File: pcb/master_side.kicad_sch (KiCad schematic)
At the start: 109 parts, among them IC1 PCA9956BTWY, J2 4P4C, J4 USB_C_Receptacle_USB2.0_16P, SW1 SW_Push_45deg, SW10 SW_Push_45deg, SW11 SW_Push_45deg, SW12 SW_Push_45deg, SW13 SW_Push_45deg, SW14 SW_Push_45deg, SW15 SW_Push_45deg, SW16 SW_Push_45deg, SW17 SW_Push_45deg, SW18 SW_Push_45deg, SW2 SW_Push_45deg, SW3 SW_Push_45deg, SW4 SW_Push_45deg, SW5 SW_Push_45deg, SW6 SW_Push_45deg, SW7 SW_Push_45deg, SW8 SW_Push_45deg, SW9 SW_Push_45deg, U1 W25Q128JVSIQ, U2 RP2040, U3 NCP1117LPST33T3G, U4 OPT3001DNPR, Y1 ABM8-272-T3

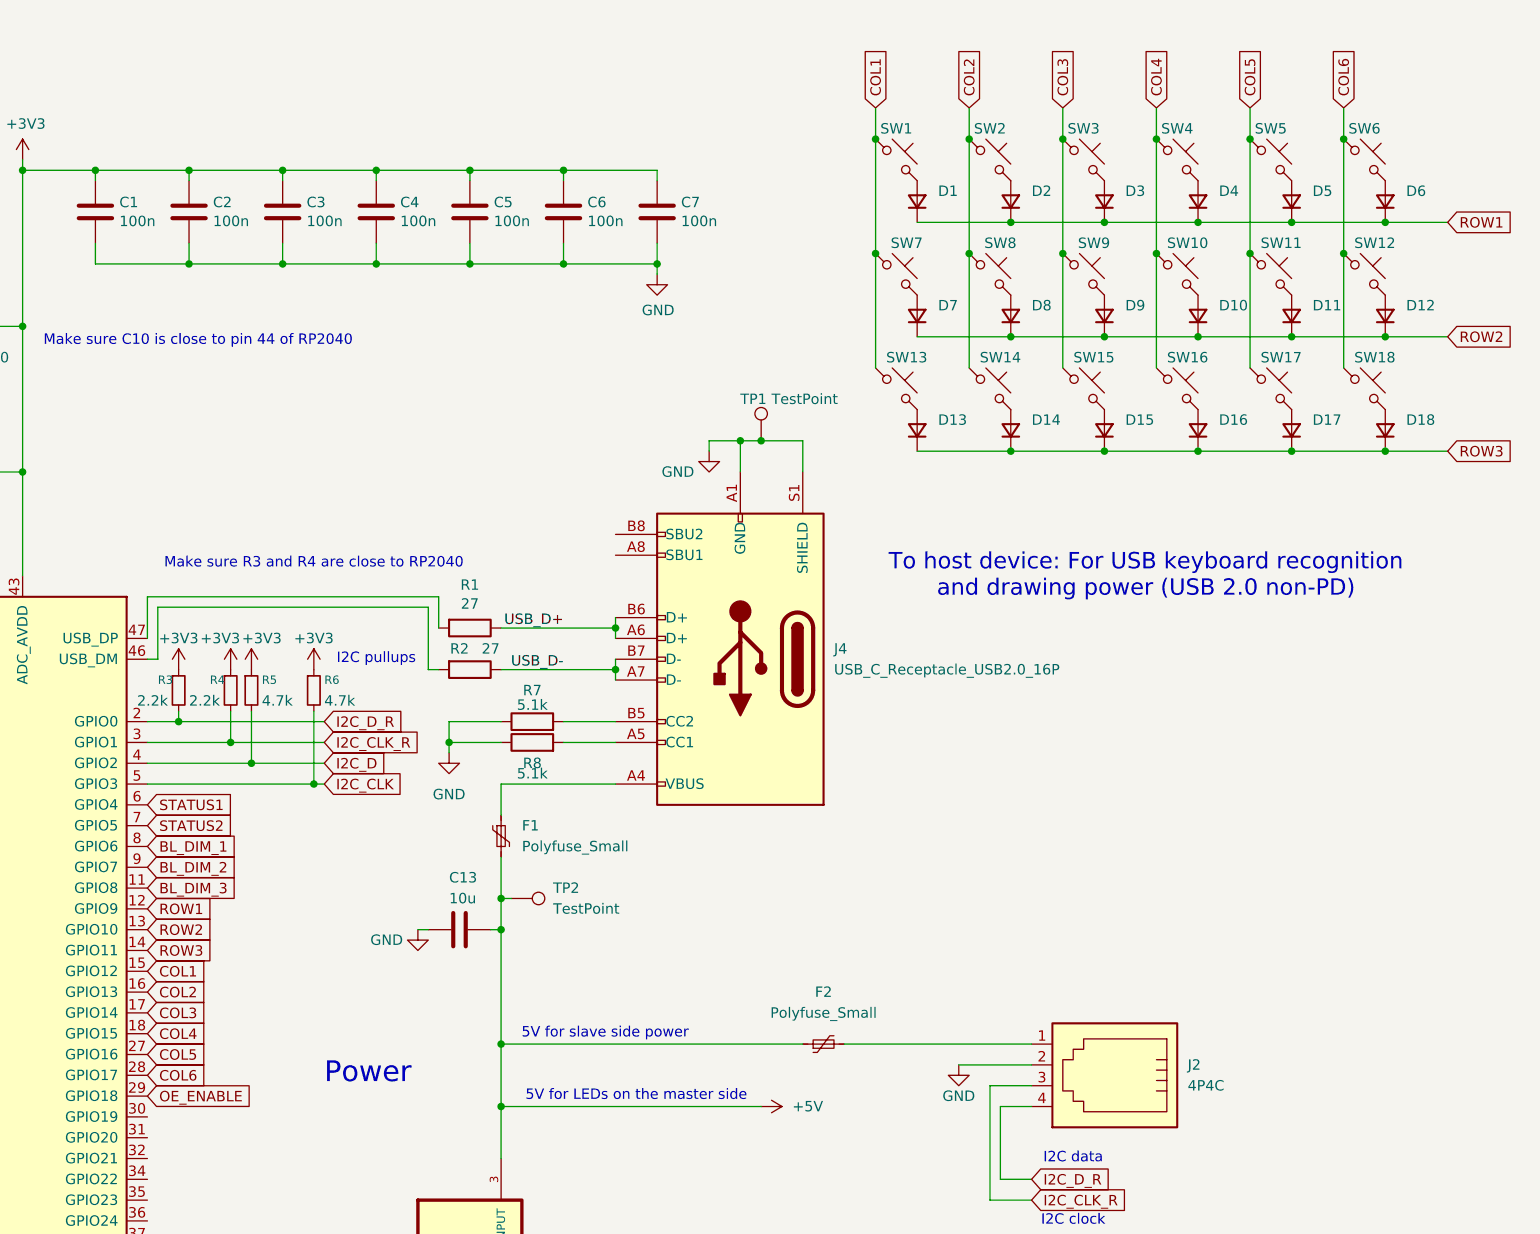
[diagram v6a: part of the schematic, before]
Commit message: fix: Fix thumb cluster key splay & Correctly align keys to outline in PCB layout
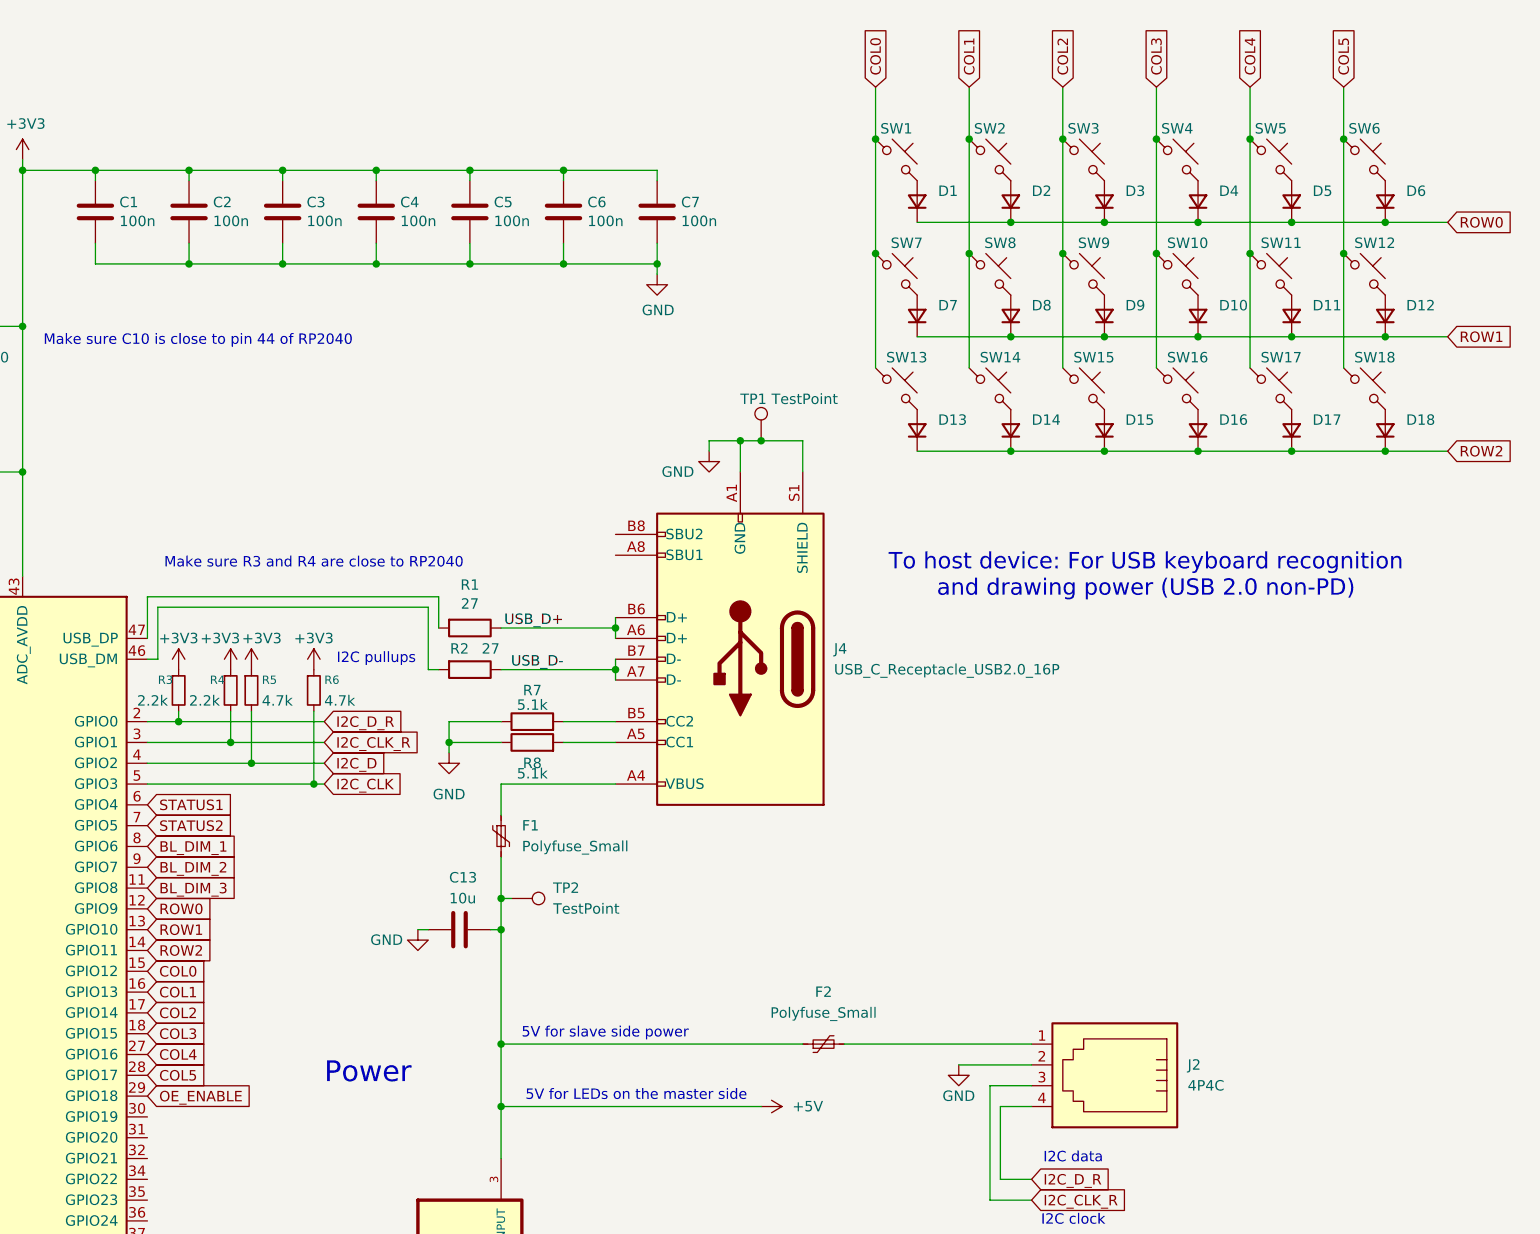
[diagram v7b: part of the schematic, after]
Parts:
- U4: DESCRIPTION Digital ambient light sensor (ALS) with high-precision huma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 -> (none)
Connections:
- net COL6 is gone; now on net COL5: SW12.1, SW18.1, SW6.1, U2.28 (GPIO17)
- net ROW3 is gone; now on net ROW2: D13.1 (K), D14.1 (K), D15.1 (K), D16.1 (K), D17.1 (K), D18.1 (K), U2.14 (GPIO11)
- net COL1: now also SW14.1, SW2.1, SW8.1, U2.16 (GPIO13); no longer SW1.1, SW13.1, SW7.1, U2.15 (GPIO12)
- net COL2: now also SW15.1, SW3.1, SW9.1, U2.17 (GPIO14); no longer SW14.1, SW2.1, SW8.1, U2.16 (GPIO13)
- net COL3: now also SW10.1, SW16.1, SW4.1, U2.18 (GPIO15); no longer SW15.1, SW3.1, SW9.1, U2.17 (GPIO14)
- net COL4: now also SW11.1, SW17.1, SW5.1, U2.27 (GPIO16); no longer SW10.1, SW16.1, SW4.1, U2.18 (GPIO15)
- net COL5: no longer SW11.1, SW17.1, SW5.1, U2.27 (GPIO16)
- net ROW1: now also D10.1 (K), D11.1 (K), D12.1 (K), D7.1 (K), D8.1 (K), D9.1 (K), U2.13 (GPIO10); no longer D1.1 (K), D2.1 (K), D3.1 (K), D4.1 (K), D5.1 (K), D6.1 (K), U2.12 (GPIO9)
- net ROW2: no longer D10.1 (K), D11.1 (K), D12.1 (K), D7.1 (K), D8.1 (K), D9.1 (K), U2.13 (GPIO10)
- new net COL0: SW1.1, SW13.1, SW7.1, U2.15 (GPIO12)
- new net ROW0: D1.1 (K), D2.1 (K), D3.1 (K), D4.1 (K), D5.1 (K), D6.1 (K), U2.12 (GPIO9)

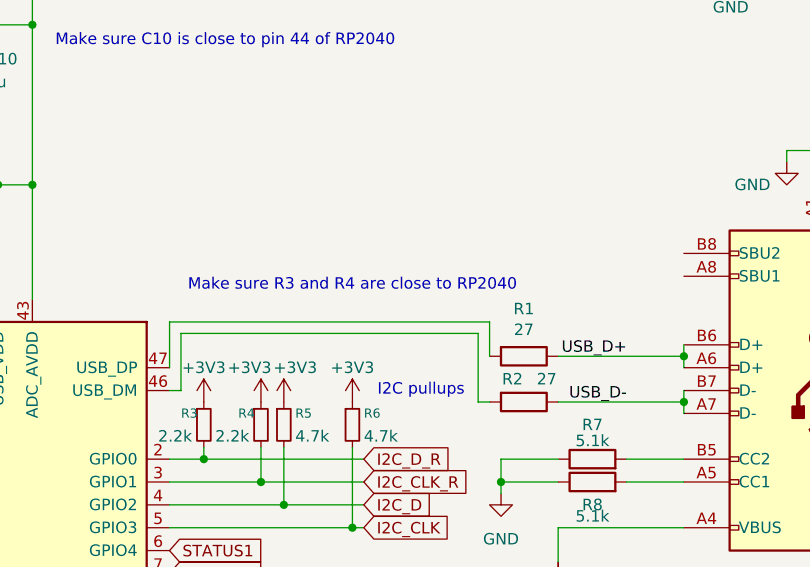
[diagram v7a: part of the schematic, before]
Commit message: fix(broken): Reroute USB
TODO:
- Fix 0402 imperial and metric confusion
- Fix DRC errors (are holes of claws of USB-C and ethernet big enough to manufacture?)
- Proper decoupling cap distribution between pins
- Manage the +1.1V and +3.3V situation (maybe create +1.1V net)
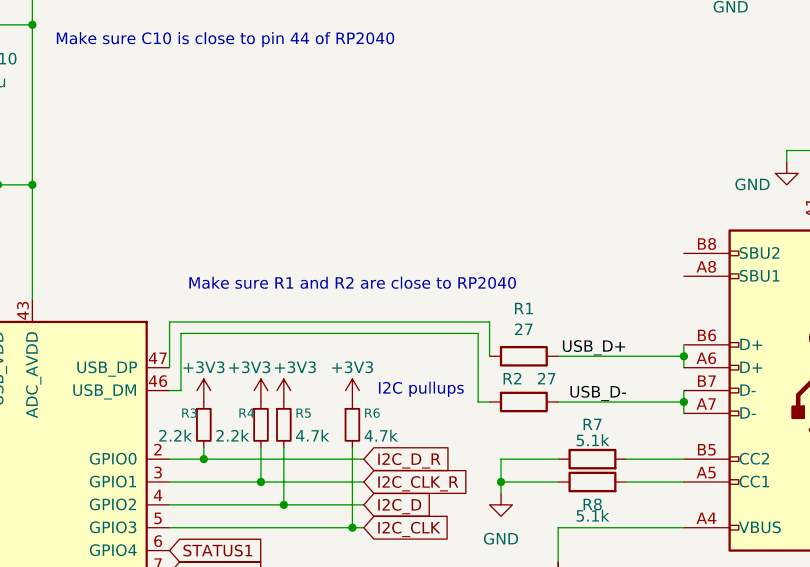
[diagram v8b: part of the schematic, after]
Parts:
- C10, C11: footprint Capacitor_SMD:C_0805_2012Metric -> Capacitor_SMD:C_01005_0402Metric
- C8, C9: footprint Capacitor_SMD:C_0805_2012Metric -> Capacitor_SMD:C_0402_1005Metric
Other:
- note added: "Make sure R1 and R2 are close to RP2040"
- note removed: "Make sure R3 and R4 are close to RP2040"
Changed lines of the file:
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@@
 		)
 	)
-	(text "Make sure R3 and R4 are close to RP2040"
+	(text "Make sure R1 and R2 are close to RP2040"
 		(exclude_from_sim no)
 		(at 240.792 85.598 0)
@@
 	)
 	(junction
-		(at 124.46 209.55)
-		(diameter 0)
-		(color 0 0 0 0)
-	)
-	(junction
 		(at 88.9 113.03)
 		(diameter 0)
@@
 	)
 	(junction
+		(at 124.46 209.55)
+		(diameter 0)
+		(color 0 0 0 0)
+	)
+	(junction
 		(at 367.03 57.15)
 		(diameter 0)
@@
 	(wire
 		(pts
-			(xy 104.14 209.55) (xy 124.46 209.55)
-		)
-		(stroke
-			(width 0)
-			(type default)
-		)
-	)
-	(wire
-		(pts
 			(xy 49.53 264.16) (xy 49.53 266.7)
 		)
@@
 	(wire
 		(pts
+			(xy 104.14 209.55) (xy 124.46 209.55)
+		)
+		(stroke
+			(width 0)
+			(type default)
+		)
+	)
+	(wire
+		(pts
 			(xy 88.9 113.03) (xy 88.9 115.57)
 		)
@@
 			)
 		)
-		(property "Footprint" "Capacitor_SMD:C_0805_2012Metric"
+		(property "Footprint" "Capacitor_SMD:C_0402_1005Metric"
 			(at 167.3352 62.23 0)
 			(hide yes)
@@
 			)
 		)
-		(property "Footprint" "Capacitor_SMD:C_0805_2012Metric"
+		(property "Footprint" "Capacitor_SMD:C_0402_1005Metric"
 			(at 178.7652 62.23 0)
 			(hide yes)
@@
 			)
 		)
-		(property "Footprint" "Capacitor_SMD:C_0805_2012Metric"
+		(property "Footprint" "Capacitor_SMD:C_01005_0402Metric"
 			(at 178.7652 77.47 0)
 			(hide yes)
@@
 			)
 		)
-		(property "Footprint" "Capacitor_SMD:C_0805_2012Metric"
+		(property "Footprint" "Capacitor_SMD:C_01005_0402Metric"
 			(at 215.5952 64.77 0)
 			(hide yes)
